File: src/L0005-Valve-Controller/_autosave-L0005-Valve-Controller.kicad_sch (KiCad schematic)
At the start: 33 parts, among them J1 Jumper_NO, P1 3220-20-0200-00, P14 647676-3, P15 647676-3, P16 647676-2, P2 140-504-415-000, P9 647676-2, U2 LMS8117AMP-3.3_NOPB, U5 Optocoupler

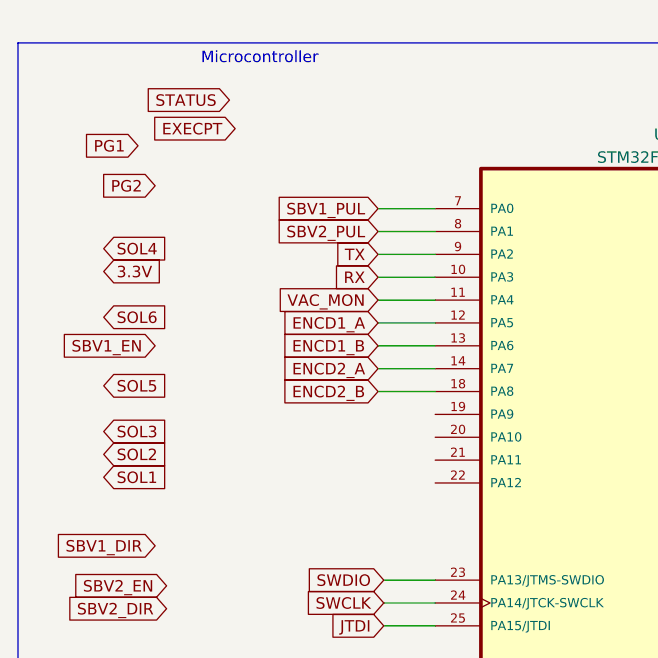
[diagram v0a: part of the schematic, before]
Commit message: added decoder to lib files
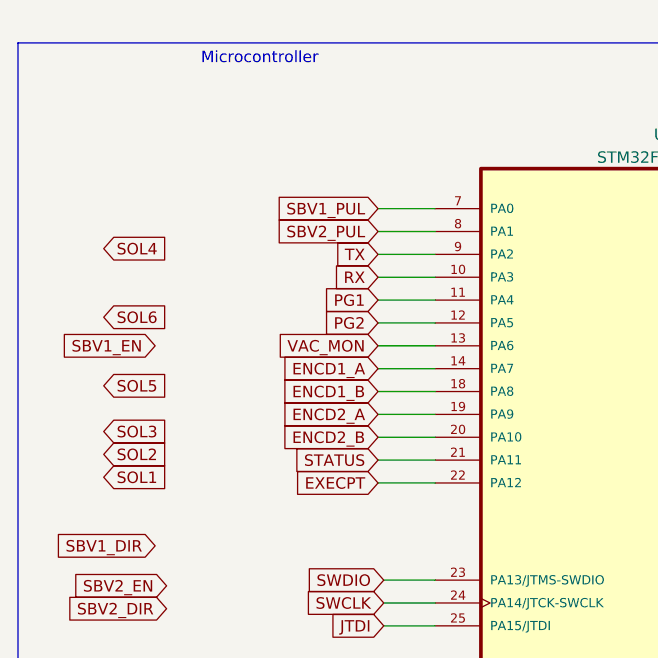
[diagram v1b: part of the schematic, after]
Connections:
- net ENCD1_A: now also U?.14 (PA7); no longer U?.12 (PA5)
- net ENCD1_B: now also U?.18 (PA8); no longer U?.13 (PA6)
- net ENCD2_A: now also U?.19 (PA9); no longer U?.14 (PA7)
- net ENCD2_B: now also U?.20 (PA10); no longer U?.18 (PA8)
- net EXECPT: now also U?.22 (PA12)
- net PG1: now also U?.11 (PA4)
- net PG2: now also U?.12 (PA5)
- net STATUS: now also U?.21 (PA11)
- net VAC_MON: now also U?.13 (PA6); no longer U?.11 (PA4)
